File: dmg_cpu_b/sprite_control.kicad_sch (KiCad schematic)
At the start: 137 parts

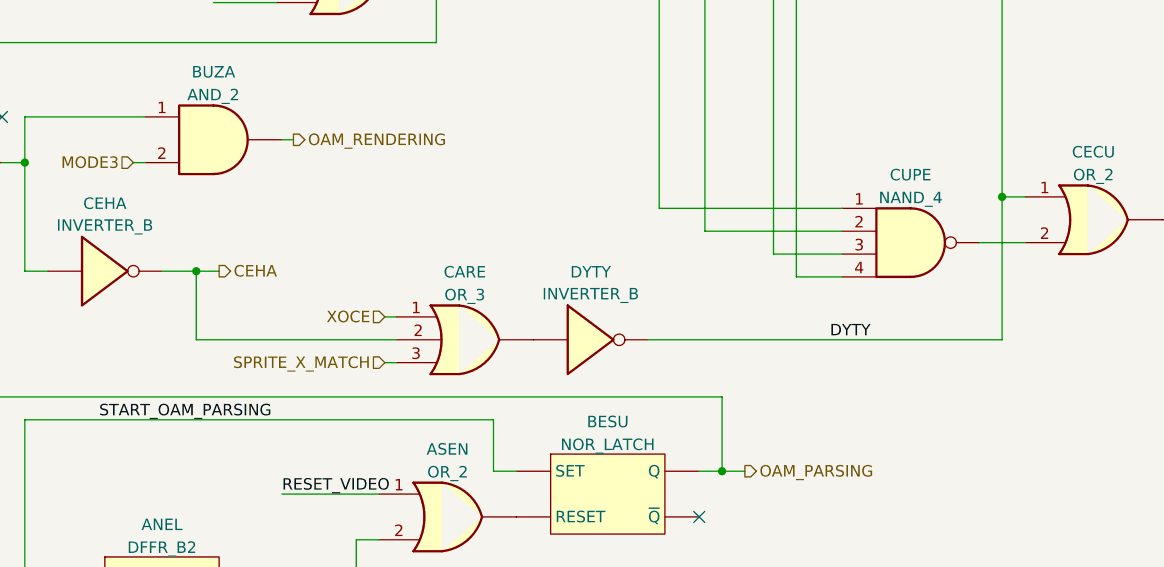
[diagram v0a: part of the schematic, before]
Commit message: More OAM sheets added.
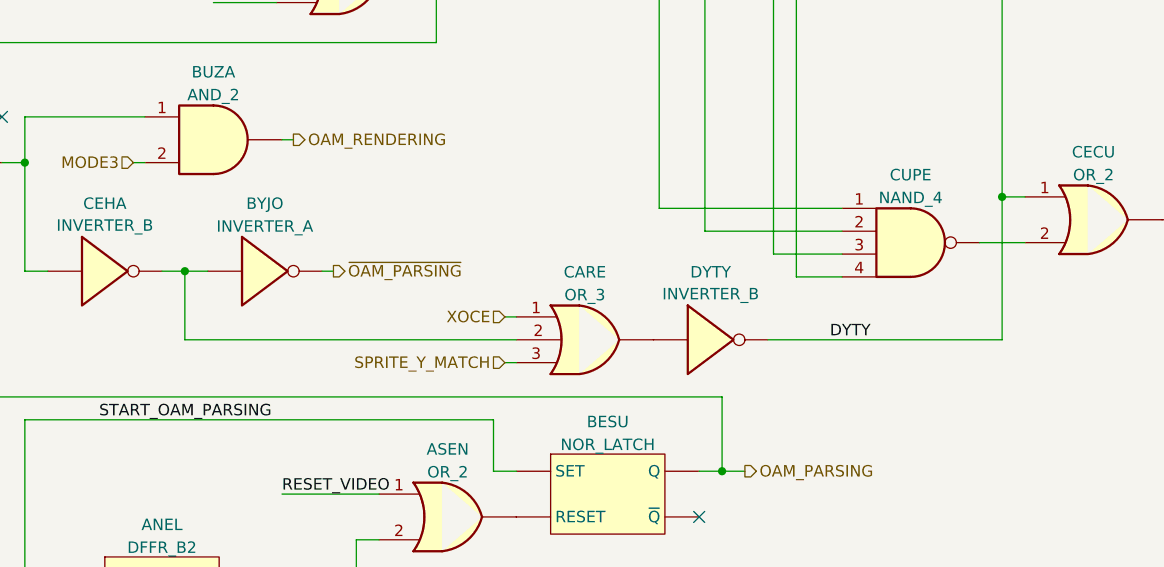
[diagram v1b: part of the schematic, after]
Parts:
- added BYJO: INVERTER_A, symbol DMG_CPU_Cells:INVERTER_A
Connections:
- net CEHA: no longer names the net of CARE.2, CEHA.2
- net CEHA: now also BYJO.1
- net SPRITE_X_MATCH renamed SPRITE_Y_MATCH
- new net ~{OAM_PARSING}: BYJO.2
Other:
- moved on the sheet: CARE, DYTY
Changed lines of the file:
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@@
   (junction (at 158.115 102.235) (diameter 0) (color 0 0 0 0)
   )
-  (junction (at 104.14 219.075) (diameter 0) (color 0 0 0 0)
-  )
   (junction (at 162.56 241.3) (diameter 0) (color 0 0 0 0)
   )
@@
   )
   (junction (at 170.18 270.51) (diameter 0) (color 0 0 0 0)
+  )
+  (junction (at 102.87 219.075) (diameter 0) (color 0 0 0 0)
   )
   (junction (at 170.815 99.06) (diameter 0) (color 0 0 0 0)
@@
     (stroke (width 0) (type default) (color 0 0 0 0))
   )
-  (wire (pts (xy 104.14 219.075) (xy 106.68 219.075))
-    (stroke (width 0) (type default) (color 0 0 0 0))
-  )
   (wire (pts (xy 256.54 259.08) (xy 185.42 259.08))
     (stroke (width 0) (type default) (color 0 0 0 0))
@@
     (stroke (width 0) (type default) (color 0 0 0 0))
   )
-  (wire (pts (xy 126.365 229.235) (xy 125.095 229.235))
+  (wire (pts (xy 139.7 229.235) (xy 138.43 229.235))
     (stroke (width 0) (type default) (color 0 0 0 0))
   )
@@
     (stroke (width 0) (type default) (color 0 0 0 0))
   )
+  (wire (pts (xy 119.38 219.075) (xy 118.11 219.075))
+    (stroke (width 0) (type default) (color 0 0 0 0))
+  )
   (wire (pts (xy 44.45 81.28) (xy 44.45 76.835))
     (stroke (width 0) (type default) (color 0 0 0 0))
@@
     (stroke (width 0) (type default) (color 0 0 0 0))
   )
-  (wire (pts (xy 104.14 219.075) (xy 104.14 226.695))
+  (wire (pts (xy 102.87 219.075) (xy 102.87 226.695))
     (stroke (width 0) (type default) (color 0 0 0 0))
   )
@@
     (stroke (width 0) (type default) (color 0 0 0 0))
   )
-  (wire (pts (xy 104.14 226.695) (xy 126.365 226.695))
+  (wire (pts (xy 102.87 226.695) (xy 139.7 226.695))
     (stroke (width 0) (type default) (color 0 0 0 0))
   )
@@
     (stroke (width 0) (type default) (color 0 0 0 0))
   )
-  (wire (pts (xy 125.095 224.155) (xy 126.365 224.155))
+  (wire (pts (xy 138.43 224.155) (xy 139.7 224.155))
     (stroke (width 0) (type default) (color 0 0 0 0))
   )
@@
     (stroke (width 0) (type default) (color 0 0 0 0))
   )
-  (wire (pts (xy 154.305 226.695) (xy 193.675 226.695))
+  (wire (pts (xy 167.64 226.695) (xy 193.675 226.695))
     (stroke (width 0) (type default) (color 0 0 0 0))
   )
@@
     (stroke (width 0) (type default) (color 0 0 0 0))
   )
+  (wire (pts (xy 102.87 219.075) (xy 105.41 219.075))
+    (stroke (width 0) (type default) (color 0 0 0 0))
+  )
   (wire (pts (xy 378.46 186.69) (xy 395.605 186.69))
     (stroke (width 0) (type default) (color 0 0 0 0))
@@
     (stroke (width 0) (type default) (color 0 0 0 0))
   )
-  (wire (pts (xy 100.33 219.075) (xy 104.14 219.075))
+  (wire (pts (xy 100.33 219.075) (xy 102.87 219.075))
     (stroke (width 0) (type default) (color 0 0 0 0))
   )
@@
     (effects (font (size 1.27 1.27)) (justify right))
   )
-  (hierarchical_label "SPRITE_X_MATCH" (shape input) (at 125.095 229.235 180)
+  (hierarchical_label "SPRITE_Y_MATCH" (shape input) (at 138.43 229.235 180)
     (effects (font (size 1.27 1.27)) (justify right))
   )
@@
     (effects (font (size 1.27 1.27)) (justify right))
   )
-  (hierarchical_label "CEHA" (shape output) (at 106.68 219.075 0)
-    (effects (font (size 1.27 1.27)) (justify left))
-  )
   (hierarchical_label "~{RESET_VIDEO}" (shape input) (at 36.195 58.42 180)
     (effects (font (size 1.27 1.27)) (justify right))
   )
+  (hierarchical_label "~{OAM_PARSING}" (shape output) (at 119.38 219.075 0)
+    (effects (font (size 1.27 1.27)) (justify left))
+  )
   (hierarchical_label "STOP_OAM_PARSING" (shape output) (at 294.64 249.555 0)
     (effects (font (size 1.27 1.27)) (justify left))
   )
-  (hierarchical_label "XOCE" (shape input) (at 125.095 224.155 180)
+  (hierarchical_label "XOCE" (shape input) (at 138.43 224.155 180)
     (effects (font (size 1.27 1.27)) (justify right))
   )
@@
     (pin "6")
   )
+  (symbol (lib_id "DMG_CPU_Cells:INVERTER_A") (at 111.76 219.075 0) (unit 1)
+    (in_bom yes) (on_board yes) (fields_autoplaced)
+    (property "Reference" "BYJO" (id 0) (at 111.76 211.5652 0))
+    (property "Value" "INVERTER_A" (id 1) (at 111.76 214.1021 0))
+    (property "Footprint" "" (id 2) (at 109.22 219.075 0)
+      (effects (font (size 1.27 1.27)) hide)
+    )
+    (property "Datasheet" "http://iceboy.a-singer.de/doc/dmg_cells.html#inv_a" (id 3) (at 113.03 226.695 0)
+      (effects (font (size 1.27 1.27)) hide)
+    )
+    (pin "1")
+    (pin "2")
+  )
   (symbol (lib_id "DMG_CPU_Cells:AND_2") (at 47.625 43.18 0) (unit 1)
     (in_bom yes) (on_board yes) (fields_autoplaced)
@@
     (pin "3")
   )
-  (symbol (lib_id "DMG_CPU_Cells:OR_3") (at 133.985 226.695 0) (unit 1)
+  (symbol (lib_id "DMG_CPU_Cells:OR_3") (at 147.32 226.695 0) (unit 1)
     (in_bom yes) (on_board yes) (fields_autoplaced)
-    (property "Reference" "CARE" (id 0) (at 133.9848 219.1852 0))
-    (property "Value" "OR_3" (id 1) (at 133.9848 221.7221 0))
-    (property "Footprint" "" (id 2) (at 133.731 226.695 0)
-      (effects (font (size 1.27 1.27)) hide)
-    )
-    (property "Datasheet" "http://iceboy.a-singer.de/doc/dmg_cells.html#or3" (id 3) (at 133.985 234.315 0)
+    (property "Reference" "CARE" (id 0) (at 147.3198 219.1852 0))
+    (property "Value" "OR_3" (id 1) (at 147.3198 221.7221 0))
+    (property "Footprint" "" (id 2) (at 147.066 226.695 0)
+      (effects (font (size 1.27 1.27)) hide)
+    )
+    (property "Datasheet" "http://iceboy.a-singer.de/doc/dmg_cells.html#or3" (id 3) (at 147.32 234.315 0)
       (effects (font (size 1.27 1.27)) hide)
     )
@@
     (pin "2")
   )
-  (symbol (lib_id "DMG_CPU_Cells:INVERTER_B") (at 147.955 226.695 0) (unit 1)
+  (symbol (lib_id "DMG_CPU_Cells:INVERTER_B") (at 161.29 226.695 0) (unit 1)
     (in_bom yes) (on_board yes)
-    (property "Reference" "DYTY" (id 0) (at 147.955 219.1852 0))
-    (property "Value" "INVERTER_B" (id 1) (at 147.955 221.615 0))
-    (property "Footprint" "" (id 2) (at 145.415 226.695 0)
-      (effects (font (size 1.27 1.27)) hide)
-    )
-    (property "Datasheet" "http://iceboy.a-singer.de/doc/dmg_cells.html#inv_b" (id 3) (at 149.225 234.315 0)
-      (effects (font (size 1.27 1.27)) hide)
-    )
+    (property "Reference" "DYTY" (id 0) (at 161.29 219.1852 0))
+    (property "Value" "INVERTER_B" (id 1) (at 161.29 221.615 0))
+    (property "Footprint" "" (id 2) (at 158.75 226.695 0)
+      (effects (font (size 1.27 1.27)) hide)
+    )
+    (property "Datasheet" "http://iceboy.a-singer.de/doc/dmg_cells.html#inv_b" (id 3) (at 162.56 234.315 0)
+      (effects (font (size 1.27 1.27)) hide)
+    )

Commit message: All sheets captured. Serious tidying is required in PPU section.
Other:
- company: (none) -> CC-BY-SA-4.0 Régis Galland & Michael Singer -- Derived work from Furrtek
- title: (none) -> DMG CPU B
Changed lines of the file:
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@@
 (kicad_sch (version 20211123) (generator eeschema)
   (paper "A3")
+  (title_block
+    (title "DMG CPU B")
+    (date "2022-05-19")
+    (rev "0")
+    (company "CC-BY-SA-4.0 Régis Galland & Michael Singer -- Derived work from Furrtek")
+    (comment 1 "https://github.com/msinger/dmg-schematics")
+  )
   (junction (at 80.645 65.405) (diameter 0) (color 0 0 0 0)
   )
